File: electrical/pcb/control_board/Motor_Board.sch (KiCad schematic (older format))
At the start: 72 parts, among them J1 ED2627-ND, J11 S7038-ND, J12 PEC10DAAN, J13 XT60-F, J14 ED2989-ND-USB, J15 XT60-F, J16 XT60-F, J17 Molex_172675-0613, J18 Molex_172675-0613, J19 Molex_172675-0613, J2 ED2627-ND, J20 Molex_172675-0613, J21 Molex_172675-0613, J22 Molex_172675-0613, J28 XT60-F, J29 XT60-F, J3 ED2627-ND, J30 XT60-F, J31 PPTC061LFBN-RC, J33 ina260_Vin, J34 ina260_8pin, J35 PPTC041LFBN-RC, J36 PPTC041LFBN-RC, J37 PPTC041LFBN-RC, J38 PPTC041LFBN-RC, J39 PPTC041LFBN-RC, J40 PPTC041LFBN-RC, J41 PPTC031LFBN-RC, J42 PPTC031LFBN-RC, J43 PPTC031LFBN-RC, J44 PPTC031LFBN-RC, J9 S7038-ND, M1 Mounting_Holes, T1 test_point, T2 test_point, T3 test_point, T4 test_point, T5 test_point, T6 test_point, y1 rover_silkscreen

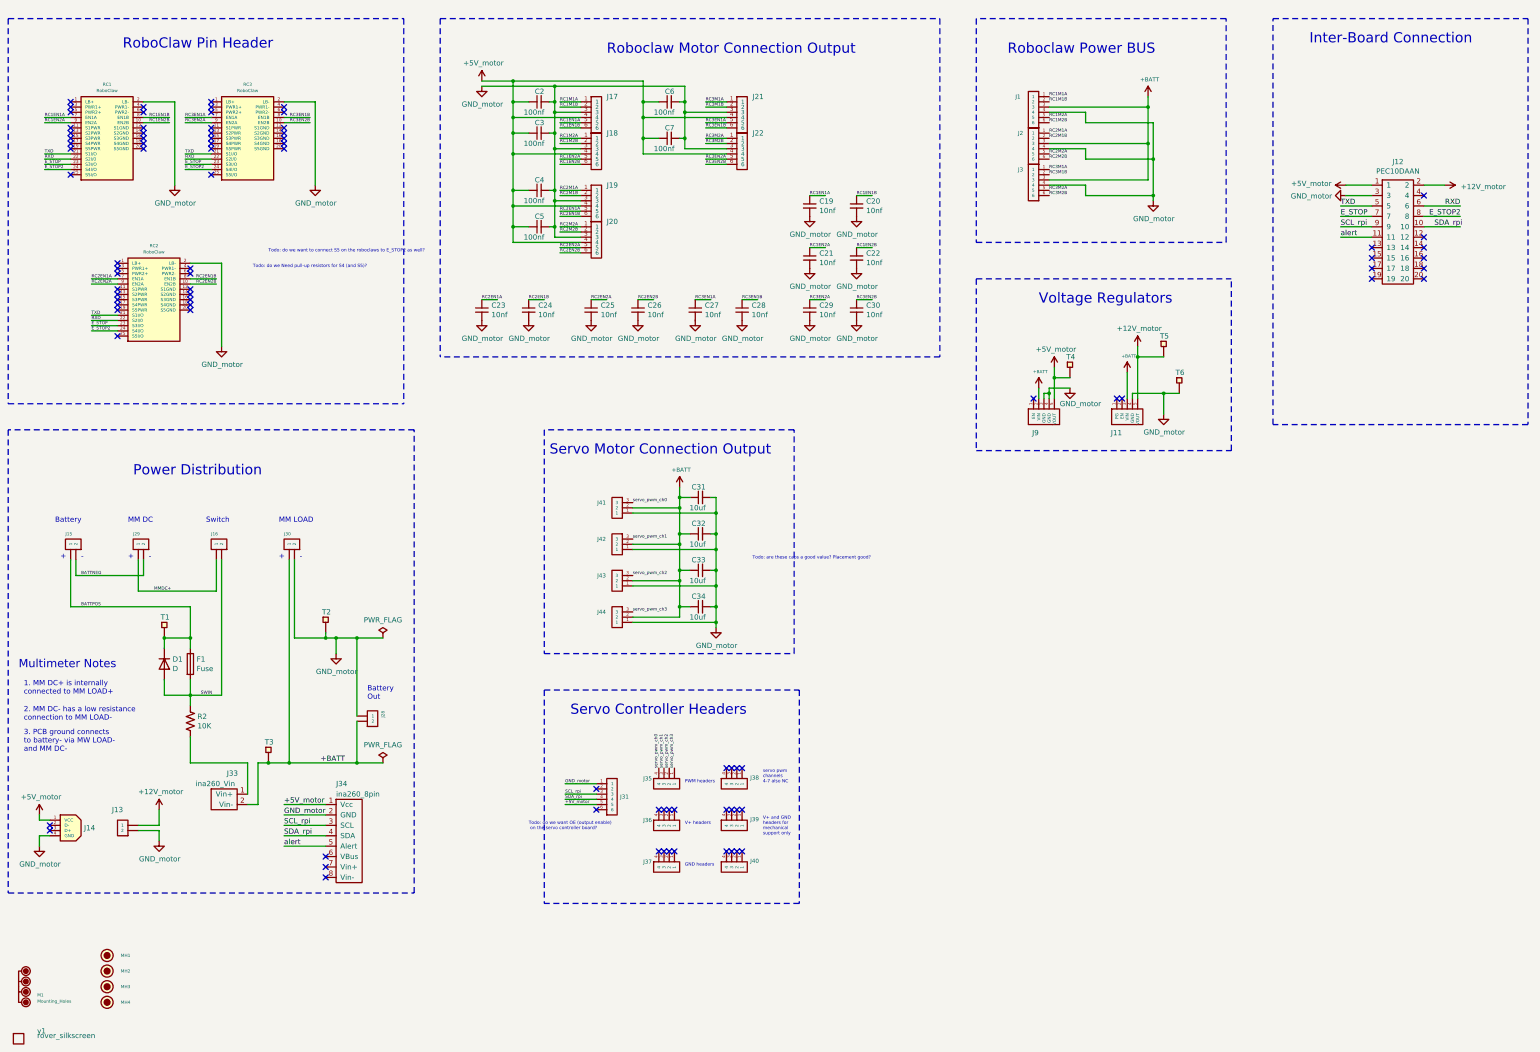
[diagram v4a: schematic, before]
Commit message: 2 WIP updates for control board after initial review
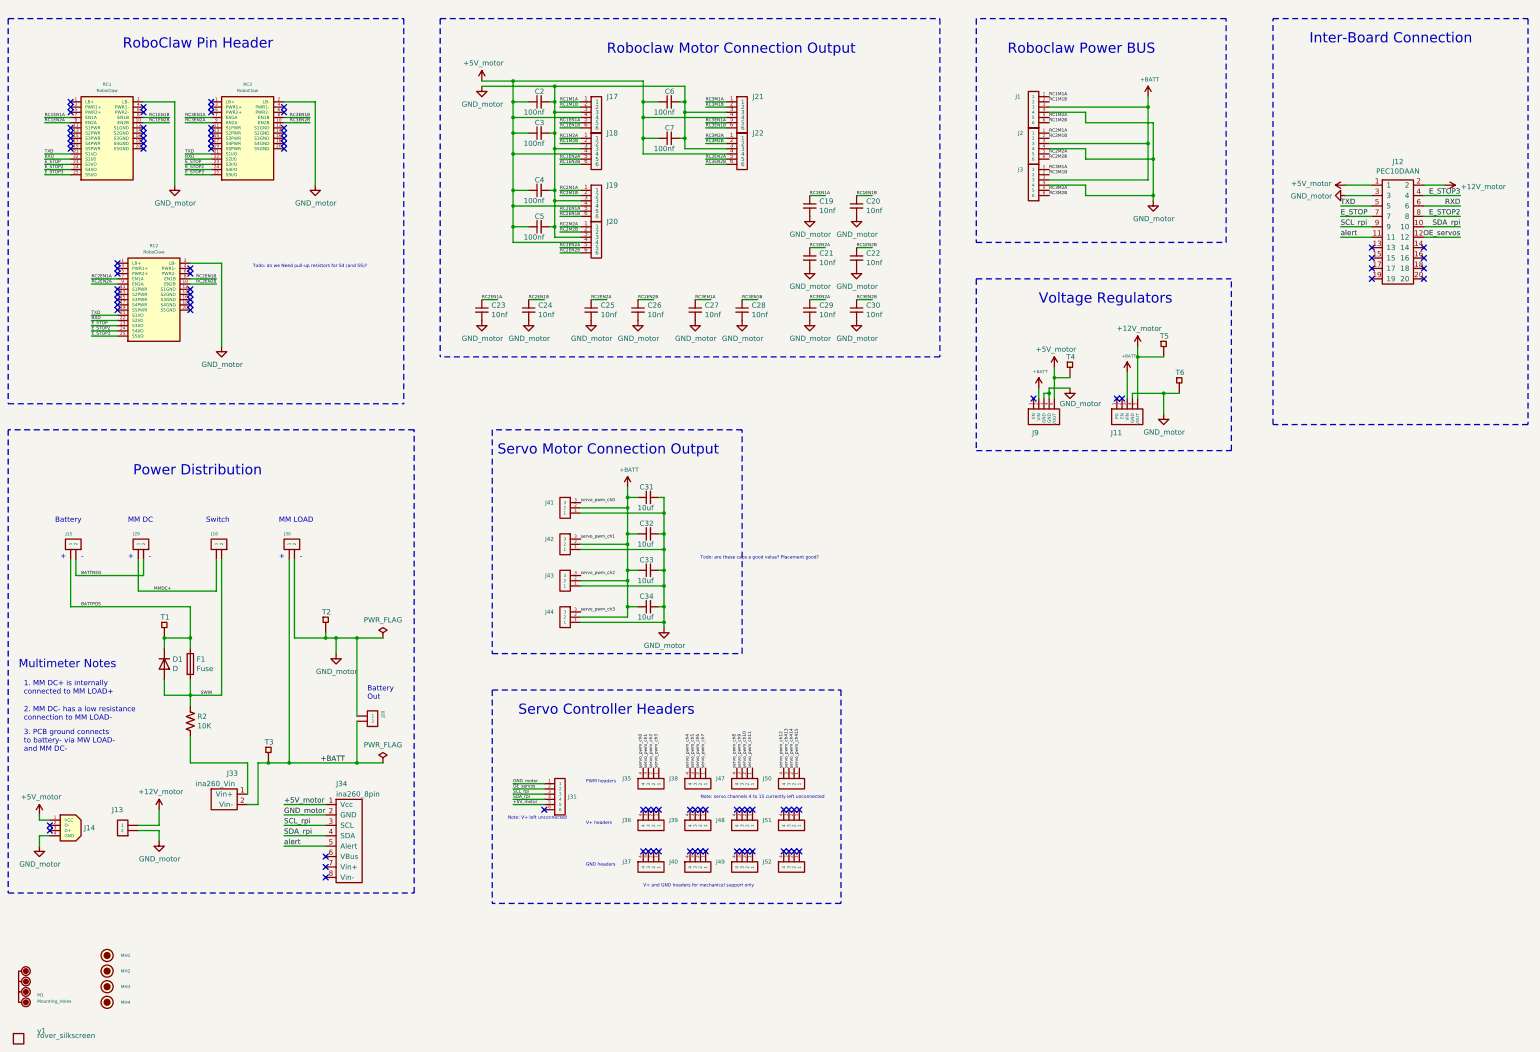
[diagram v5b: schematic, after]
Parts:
- added J47, J48, J49, J50, J51, J52: PPTC041LFBN-RC, symbol JPL_Robotics_Lib:PPTC041LFBN-RC
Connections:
- net labels added: E_STOP3, OE_servos, servo_pwm_ch10, servo_pwm_ch11, servo_pwm_ch12, servo_pwm_ch4, servo_pwm_ch413, servo_pwm_ch414, servo_pwm_ch415, servo_pwm_ch5, servo_pwm_ch6, servo_pwm_ch7, servo_pwm_ch8, servo_pwm_ch9
- wire segments 249 -> 255
- no-connect marks 88 -> 94
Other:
- note added: "Note: V+ left unconnected"
- note added: "Note: servo channels 4 to 15 currently left unconnected"
- note added: "V+ and GND headers for mechanical support only"
- note removed: "Todo: do we want OE (output enable)\n on the servo controller board?"
- note removed: "Todo: do we want to connect S5 on the roboclaws to E_STOP2 as well?\n"
- note removed: "V+ and GND \nheaders for \nmechanical \nsupport only"
- note removed: "servo pwm\nchannels \n4-7 also NC"
- moved on the sheet: C31, C32, C33, C34, J31, J35, J36, J37, J38, J39, J40, J41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

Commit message: 3 WIP post initial updates from eric
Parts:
- J12: value PEC10DAAN -> PPTC102LFBN-RC; footprint JPL Robotics:PEC10DAAN -> JPL Robotics:PPTC102LFBN-RC; symbol JPL_Robotics_Lib:PEC10DAAN -> JPL_Robotics_Lib:PPTC102LFBN-RC
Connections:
- net labels added: OEservos
- net labels removed: OE_servos
- wire segments 255 -> 258
- no-connect marks 94 -> 89
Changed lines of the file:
@@
 Connection ~ 4350 6900
 Wire Wire Line
-	14600 2550 14800 2550
-Wire Wire Line
-	13800 2850 14100 2850
-Wire Wire Line
-	13800 2750 14100 2750
-Wire Wire Line
-	13850 2650 14100 2650
+	13800 3150 14100 3150
+Wire Wire Line
+	13800 2650 14100 2650
+Wire Wire Line
+	13850 2750 14100 2750
 Wire Wire Line
 	13850 2550 14100 2550
-Text Label 13800 2850 0    50   ~ 0
+Text Label 13800 3150 0    50   ~ 0
 E_STOP
-Text Label 14950 2750 2    50   ~ 0
+Text Label 14950 2650 2    50   ~ 0
 RXD
-Text Label 13800 2750 0    50   ~ 0
+Text Label 13800 2650 0    50   ~ 0
 TXD
 Text Notes 13500 1200 0    98   ~ 0
@@
 Wire Notes Line style solid rgb(0, 0, 0)
 	15600 950  15600 4850
-NoConn ~ 14600 3150
-NoConn ~ 14600 3250
-NoConn ~ 14600 3350
 NoConn ~ 14600 3450
-NoConn ~ 14100 3150
 NoConn ~ 14100 3250
-NoConn ~ 14100 3350
 NoConn ~ 14100 3450
 $Comp
@@
 L JPL_Robotics_Lib:GND_motor #PWR0141
 U 1 1 6180C6BB
-P 13850 2650
-F 0 "#PWR0141" H 13850 2400 50  0001 C CNN
-F 1 "GND_motor" V 13855 2319 50  0000 C CNN
-F 2 "" H 13850 2650 50  0001 C CNN
-F 3 "" H 13850 2650 50  0001 C CNN
-	1    13850 2650
+P 13850 2750
+F 0 "#PWR0141" H 13850 2500 50  0001 C CNN
+F 1 "GND_motor" V 13855 2419 50  0000 C CNN
+F 2 "" H 13850 2750 50  0001 C CNN
+F 3 "" H 13850 2750 50  0001 C CNN
+	1    13850 2750
 	0    1    1    0
 $EndComp
@@
 L JPL_Robotics_Lib:+12V_motor #PWR0143
 U 1 1 618B58EE
-P 14800 2550
-F 0 "#PWR0143" H 14800 2400 50  0001 C CNN
-F 1 "+12V_motor" V 14815 2920 50  0000 C CNN
-F 2 "" H 14800 2550 50  0001 C CNN
-F 3 "" H 14800 2550 50  0001 C CNN
-	1    14800 2550
+P 14950 2950
+F 0 "#PWR0143" H 14950 2800 50  0001 C CNN
+F 1 "+12V_motor" V 14965 3320 50  0000 C CNN
+F 2 "" H 14950 2950 50  0001 C CNN
+F 3 "" H 14950 2950 50  0001 C CNN
+	1    14950 2950
 	0    1    1    0
 $EndComp
@@
 	5150 950  5150 4200
 Wire Wire Line
-	14600 2850 14950 2850
-Text Label 14950 2850 2    50   ~ 0
+	14600 3150 14950 3150
+Text Label 14950 3150 2    50   ~ 0
 E_STOP2
 Wire Wire Line
-	14600 2750 14950 2750
+	14600 2650 14950 2650
 Wire Wire Line
 	1600 2400 1350 2400
@@
 	3650 8600 4050 8600
 Wire Wire Line
-	14100 2950 13800 2950
-Text Label 13800 2950 0    50   ~ 0
+	14100 2850 13800 2850
+Text Label 13800 2850 0    50   ~ 0
 SCL_rpi
 Wire Wire Line
-	14600 2950 14950 2950
-Text Label 14950 2950 2    50   ~ 0
+	14600 2850 14950 2850
+Text Label 14950 2850 2    50   ~ 0
 SDA_rpi
 Wire Wire Line
@@
 NoConn ~ 4050 9200
 Wire Wire Line
-	14100 3050 13800 3050
-Text Label 13800 3050 0    50   ~ 0
+	14100 3350 13800 3350
+Text Label 13800 3350 0    50   ~ 0
 alert
 Wire Wire Line
@@
 NoConn ~ 2050 3300
 Wire Wire Line
-	14600 2650 14950 2650
-Text Label 14950 2650 2    50   ~ 0
+	14600 3250 14950 3250
+Text Label 14950 3250 2    50   ~ 0
 E_STOP3
 $Comp
@@
 	6150 8350 5850 8350
 Text Label 5850 8350 0    30   ~ 0
-OE_servos
+OEservos
 NoConn ~ 6150 8550
 Text Notes 5800 8650 0    31   ~ 0
 Note: V+ left unconnected
-$Comp
-L JPL_Robotics_Lib:PEC10DAAN J12
-U 1 1 6099FCA6
-P 14350 2400
-F 0 "J12" H 14350 2475 50  0000 C CNN
-F 1 "PEC10DAAN" H 14350 2384 50  0000 C CNN
-F 2 "JPL Robotics:PEC10DAAN" H 14550 2400 50  0001 C CNN
-F 3 "" H 14550 2400 50  0001 C CNN
-	1    14350 2400
-	1    0    0    -1
-$EndComp
-Wire Wire Line
-	14600 3050 14950 3050
-Text Label 14950 3050 2    50   ~ 0
-OE_servos
 $Comp
 L JPL_Robotics_Lib:PPTC041LFBN-RC J48
@@
 Text Notes 7650 8450 0    31   ~ 0
 Note: servo channels 4 to 15 currently left unconnected
+$Comp
+L JPL_Robotics_Lib:GND_motor #PWR?
+U 1 1 60FDA9F9
+P 14900 2750
+F 0 "#PWR?" H 14900 2500 50  0001 C CNN
+F 1 "GND_motor" V 14905 2419 50  0000 C CNN
+F 2 "" H 14900 2750 50  0001 C CNN
+F 3 "" H 14900 2750 50  0001 C CNN
+	1    14900 2750
+	0    -1   -1   0
+$EndComp
+Wire Wire Line
+	14600 2750 14900 2750
+$Comp
+L JPL_Robotics_Lib:+5V_motor #PWR?
+U 1 1 610774EE
+P 14950 2550
+F 0 "#PWR?" H 14950 2400 50  0001 C CNN
+F 1 "+5V_motor" V 14965 2882 50  0000 C CNN
+F 2 "" H 14950 2550 50  0001 C CNN
+F 3 "" H 14950 2550 50  0001 C CNN
+	1    14950 2550
+	0    1    1    0
+$EndComp
+Wire Wire Line
+	14600 2550 14950 2550
+Wire Wire Line
+	14950 2950 14600 2950
+$Comp
+L JPL_Robotics_Lib:+12V_motor #PWR?
+U 1 1 6112A222
+P 13800 2950
+F 0 "#PWR?" H 13800 2800 50  0001 C CNN
+F 1 "+12V_motor" V 13815 3320 50  0000 C CNN
+F 2 "" H 13800 2950 50  0001 C CNN
+F 3 "" H 13800 2950 50  0001 C CNN
+	1    13800 2950
+	0    -1   -1   0
+$EndComp
+Wire Wire Line
+	13800 2950 14100 2950
+$Comp
+L JPL_Robotics_Lib:PPTC102LFBN-RC J12
+U 1 1 6099FCA6
+P 14350 2400
+F 0 "J12" H 14350 2475 50  0000 C CNN
+F 1 "PPTC102LFBN-RC" H 14350 2384 50  0000 C CNN
+F 2 "JPL Robotics:PPTC102LFBN-RC" H 14550 2400 50  0001 C CNN
+F 3 "" H 14550 2400 50  0001 C CNN
+	1    14350 2400
+	1    0    0    -1
+$EndComp
+Wire Wire Line
+	14600 3350 14950 3350
+Text Label 14950 3350 2    50   ~ 0
+OEservos
 $EndSCHEMATC

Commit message: 4 WIP first pass through david comments
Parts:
- added J53: PEC08SAAN, symbol JPL_Robotics_Lib:PEC08SAAN
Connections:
- wire segments 258 -> 265
- no-connect marks 89 -> 92
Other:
- note added: "Note: header is female, to prevent accidental shorts"
- note added: "Test Pin Header"
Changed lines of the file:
@@
 Note: servo channels 4 to 15 currently left unconnected
 $Comp
-L JPL_Robotics_Lib:GND_motor #PWR?
+L JPL_Robotics_Lib:GND_motor #PWR048
 U 1 1 60FDA9F9
 P 14900 2750
-F 0 "#PWR?" H 14900 2500 50  0001 C CNN
+F 0 "#PWR048" H 14900 2500 50  0001 C CNN
 F 1 "GND_motor" V 14905 2419 50  0000 C CNN
 F 2 "" H 14900 2750 50  0001 C CNN
@@
 	14600 2750 14900 2750
 $Comp
-L JPL_Robotics_Lib:+5V_motor #PWR?
+L JPL_Robotics_Lib:+5V_motor #PWR049
 U 1 1 610774EE
 P 14950 2550
-F 0 "#PWR?" H 14950 2400 50  0001 C CNN
+F 0 "#PWR049" H 14950 2400 50  0001 C CNN
 F 1 "+5V_motor" V 14965 2882 50  0000 C CNN
 F 2 "" H 14950 2550 50  0001 C CNN
@@
 	14950 2950 14600 2950
 $Comp
-L JPL_Robotics_Lib:+12V_motor #PWR?
+L JPL_Robotics_Lib:+12V_motor #PWR047
 U 1 1 6112A222
 P 13800 2950
-F 0 "#PWR?" H 13800 2800 50  0001 C CNN
+F 0 "#PWR047" H 13800 2800 50  0001 C CNN
 F 1 "+12V_motor" V 13815 3320 50  0000 C CNN
 F 2 "" H 13800 2950 50  0001 C CNN
@@
 Text Label 14950 3350 2    50   ~ 0
 OEservos
+Wire Notes Line style solid rgb(0, 0, 0)
+	11650 5300 9250 5300
+Text Notes 9850 5550 0    98   ~ 0
+Test Pin Header
+Wire Notes Line
+	9250 5300 9250 6800
+Wire Notes Line
+	9250 6800 11650 6800
+Wire Notes Line
+	11650 6800 11650 5300
+Text Label 9850 6100 0    50   ~ 0
+TXD
+NoConn ~ 10300 6500
+Wire Wire Line
+	9850 6200 10300 6200
+Wire Wire Line
+	9850 6100 10300 6100
+Text Label 9850 6200 0    50   ~ 0
+RXD
+Wire Wire Line
+	9850 6400 10300 6400
+Wire Wire Line
+	9850 6300 10300 6300
+Wire Wire Line
+	9850 6000 10300 6000
+Wire Wire Line
+	9850 5900 10300 5900
+Wire Wire Line
+	9850 5800 10300 5800
+Text Label 9850 5900 0    50   ~ 0
++12V_motor
+Text Label 9850 5800 0    50   ~ 0
++5V_motor
+Text Label 9850 6400 0    50   ~ 0
+SDA_rpi
+Text Label 9850 6300 0    50   ~ 0
+SCL_rpi
+Text Label 9850 6000 0    50   ~ 0
+GND_motor
+$Comp
+L JPL_Robotics_Lib:PEC08SAAN J53
+U 1 1 6127184F
+P 10650 5650
+F 0 "J53" H 10578 5201 50  0000 L CNN
+F 1 "PEC08SAAN" H 10578 5110 50  0000 L CNN
+F 2 "" H 10700 5650 50  0001 C CNN
+F 3 "" H 10700 5650 50  0001 C CNN
+	1    10650 5650
+	1    0    0    -1
+$EndComp
+Text Notes 9600 6700 0    31   ~ 0
+Note: header is female, to prevent accidental shorts
+NoConn ~ 14100 3050
+NoConn ~ 14600 3050
 $EndSCHEMATC
